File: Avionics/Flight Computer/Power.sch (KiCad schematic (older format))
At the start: 0 parts

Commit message: Lots of power tree and layout work
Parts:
- added C45: 1n, Capacitors_SMD:C_0402, symbol C
- added C46: 2.2u, Capacitors_SMD:C_0402, symbol C
- added C47: 0.1u, Capacitors_SMD:C_0402, symbol C
- added C48, C49: 10u, Capacitors_SMD:C_1206, symbol C
- added C50: 2.2u, Capacitors_SMD:C_0805, symbol C
- added C51, C52: 22u, Capacitors_SMD:C_1206, symbol C
- added L16, L17: 744316220, Inductors_SMD:L_Wuerth_HCI-5040, symbol L
- added R10: 20k, Resistors_SMD:R_0402, symbol R
- added R11: 12k, Resistors_SMD:R_0402, symbol R
- added R12: 100k, Resistors_SMD:R_0402, symbol R
- added R13: 10k, Resistors_SMD:R_0402, symbol R
- added U8: MAX17243, Housings_DFN_QFN:QFN-20-1EP_5x5mm_Pitch0.65mm, symbol MAX17243
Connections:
- new net: R11.1, U8.1 (FOSC)
- new net: C49.1, C50.1, L16.2, R12.1, U8.10 (SUP), U8.8 (SUPSW), U8.9 (SUPSW)
- new net: C47.2, U8.15 (BST)
- new net: C47.1, L17.2, U8.16 (LX), U8.17 (LX), U8.18 (LX)
- new net: R10.1, U8.4 (COMP)
- new net: C45.1, R10.2
- new net +3V3: C51.1, C52.1, L17.1, R13.1, U8.2 (OUT)
- new net BIAS: C46.1, U8.12 (SPS), U8.3 (FB), U8.5 (BIAS)
- new net GND: C45.2, C46.2, C48.2, C49.2, C50.2, C51.2, C52.2, R11.2, U8.13 (PGND), U8.14 (PGND), U8.20 (FSYNC), U8.21 (PGND_EP), U8.6 (AGND)
- new net PGOOD: R13.2, U8.11 (PGOOD)
- new net VIN: C48.1, L16.1
- new net ~SHDN: R12.2, U8.7 (EN)
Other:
- note added: "2.2uH, 5040 package Wurth"
- note added: "FSYNC tied low to enable pulse-frequency modulation"
- note added: "Input caps must be >=50V rated"
- note added: "Input pi filter (helps block ESC noise)"
- note added: "Note that SHDN is pulled high to VIN"
- note added: "R11 sets oscillation frequency to 2.2MHz"
- note added: "SPS and FB tied to bias to enable 3.3V spread spectrum mode."
- note added: "TODO: Tune input filter"

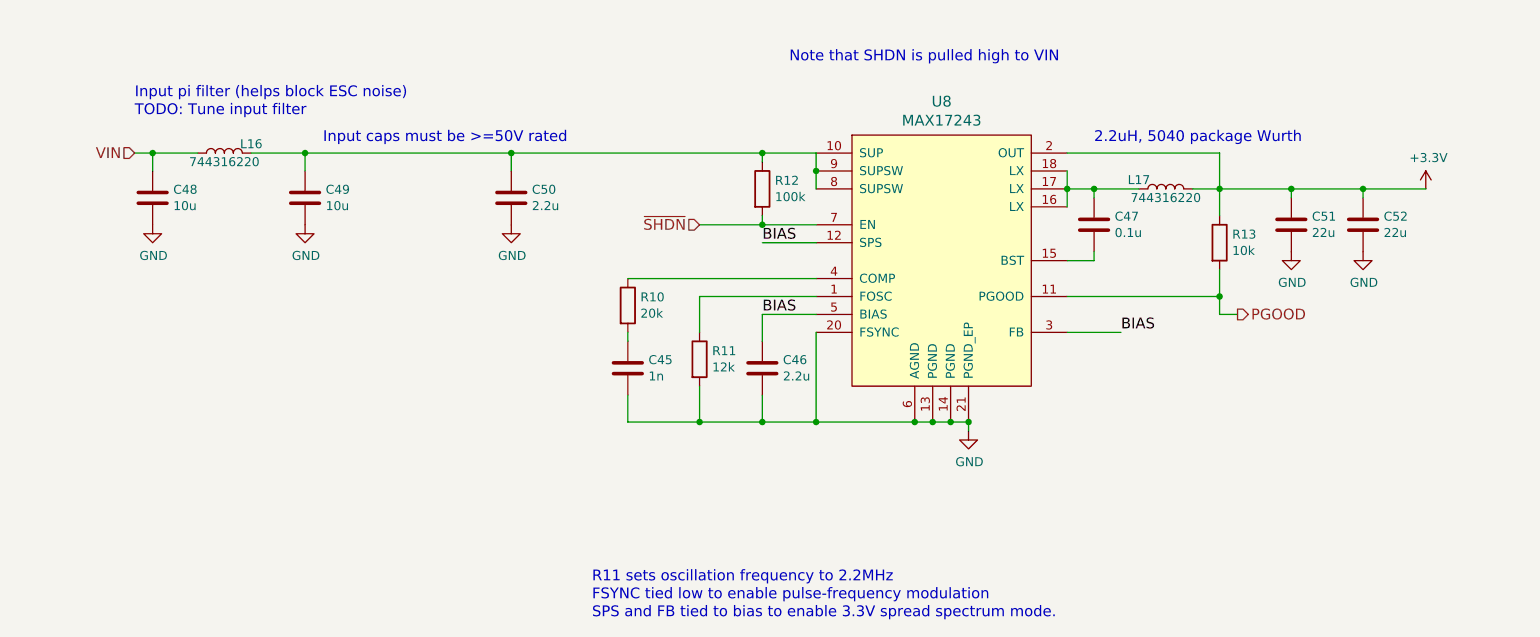
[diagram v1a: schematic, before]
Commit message: Restarted initial layout and cleaned up decoupling/RF layout.
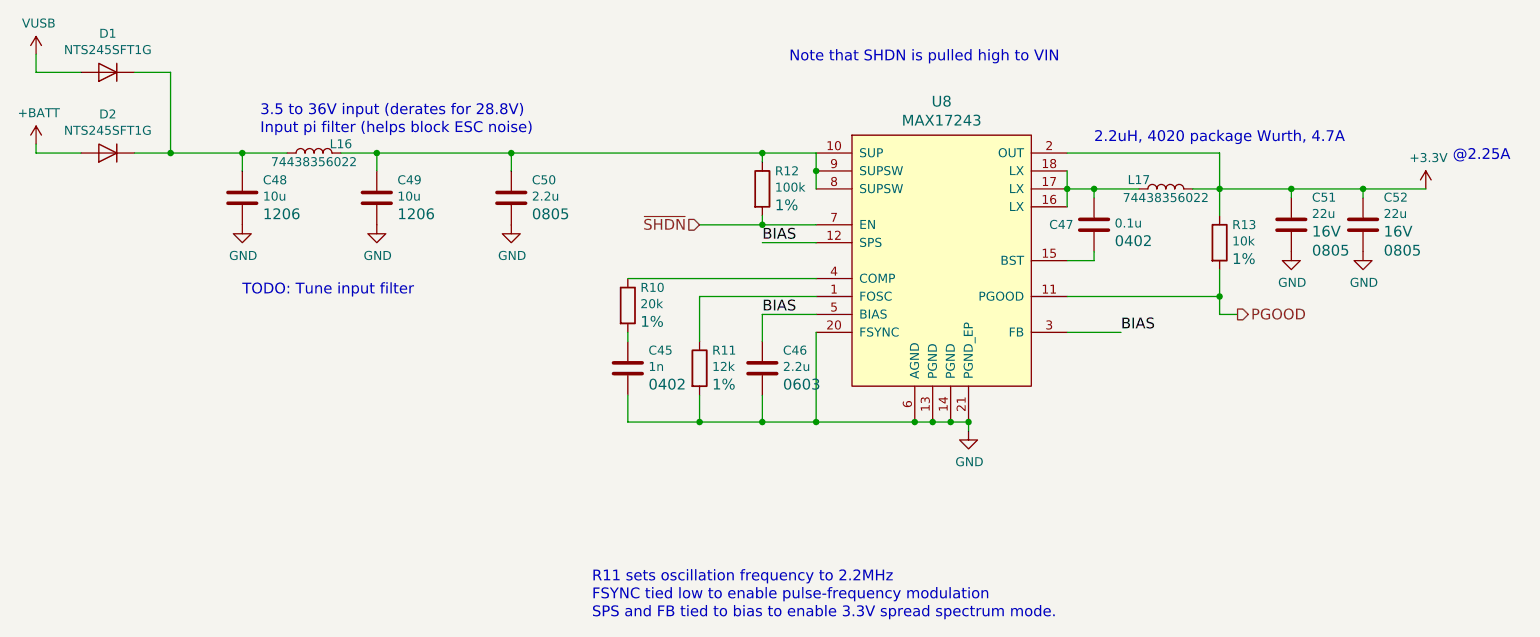
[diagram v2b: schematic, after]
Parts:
- added D1, D2: NTS245SFT1G, Diodes_SMD:D_SOD-123F, symbol D
- C45, C47: Package (none) -> 0402; Tolerance (none) -> 20%; Type (none) -> X7R; Voltage (none) -> 50V
- C46: footprint Capacitors_SMD:C_0402 -> Capacitors_SMD:C_0603; Package (none) -> 0603; Tolerance (none) -> 20%; Type (none) -> X7R; Voltage (none) -> 16V
- C48, C49: Package (none) -> 1206; Tolerance (none) -> 20%; Type (none) -> X7R; Voltage (none) -> 50V
- C50: Package (none) -> 0805; Tolerance (none) -> 20%; Type (none) -> X7R; Voltage (none) -> 50V
- C51, C52: footprint Capacitors_SMD:C_1206 -> Capacitors_SMD:C_0805; Package (none) -> 0805; Tolerance (none) -> 20%; Type (none) -> X7R; Voltage (none) -> 16V
- L16, L17: value 744316220 -> 74438356022; footprint Inductors_SMD:L_Wuerth_HCI-5040 -> Inductors_SMD:L_Wuerth_MAPI-4020
- R10, R11, R12, R13: Material (none) -> Thin Film; Package (none) -> 0402; Power (none) -> 0.062W; Tolerance (none) -> 1%; Voltage (none) -> 50V
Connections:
- net VIN: no longer names the net of C48.1, L16.1
- net VIN: now also D1.1 (K), D2.1 (K)
- new net +BATT: D2.2 (A)
- new net VUSB: D1.2 (A)
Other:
- note added: "2.2uH, 4020 package Wurth, 4.7A"
- note added: "3.5 to 36V input (derates for 28.8V)"
- note added: "@2.25A"
- note removed: "2.2uH, 5040 package Wurth"
- note removed: "Input caps must be >=50V rated"
- moved on the sheet: L16

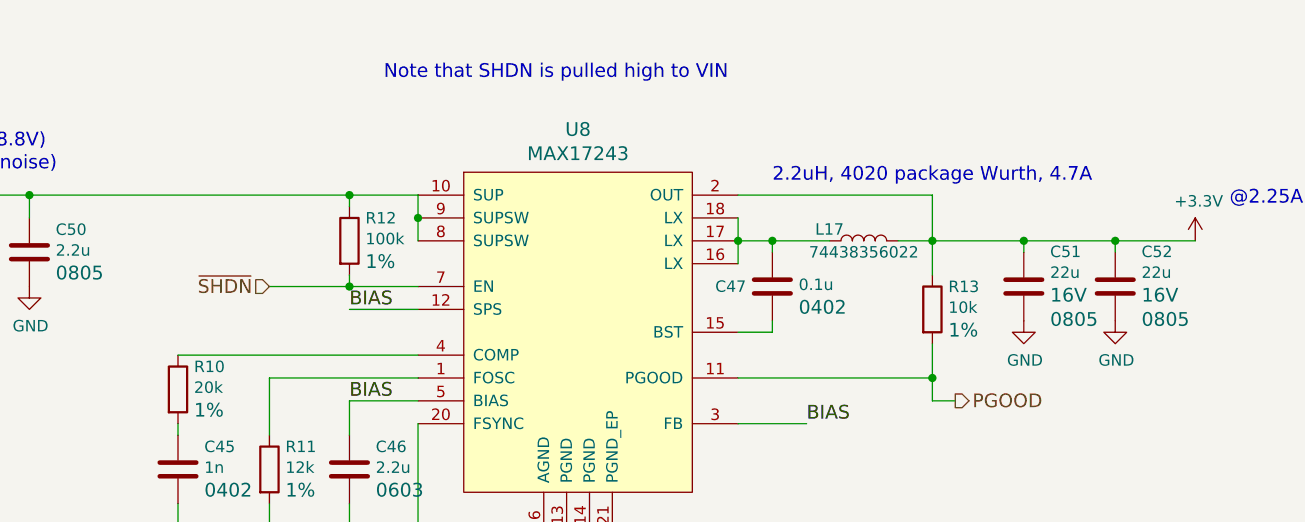
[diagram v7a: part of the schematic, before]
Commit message: Finished routing and DRC check.
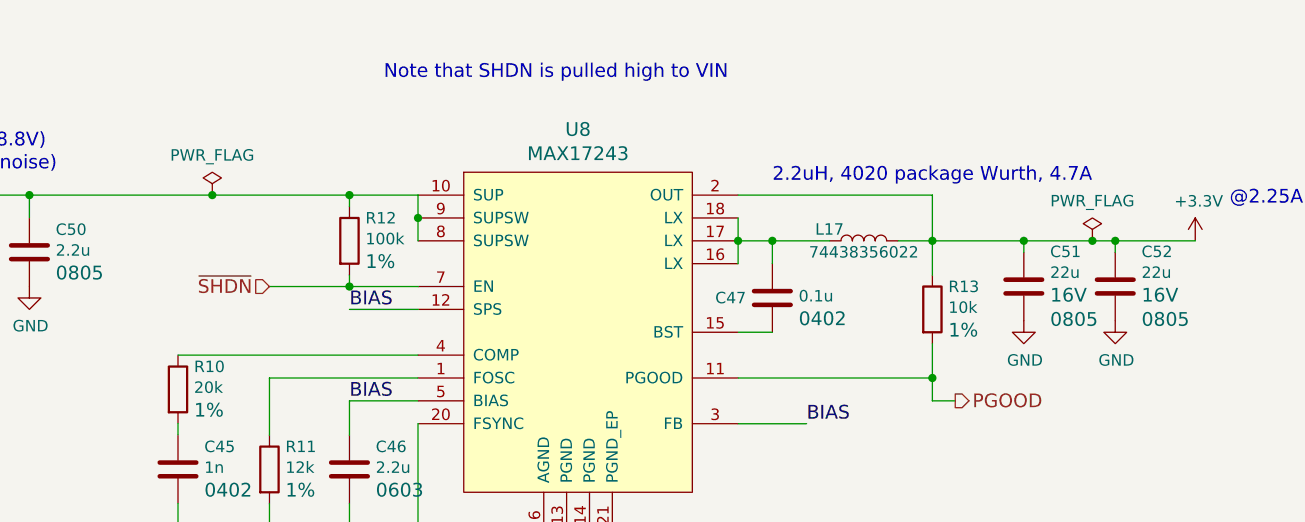
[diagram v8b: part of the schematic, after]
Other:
- moved on the sheet: C47
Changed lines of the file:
@@
 Text Notes 6750 2850 0    60   ~ 0
 2.2uH, 4020 package Wurth, 4.7A
-$Comp
-L MAX17243 U8
-U 1 1 58AB8A07
-P 5900 3500
-F 0 "U8" H 5900 4387 60  0000 C CNN
-F 1 "MAX17243" H 5900 4281 60  0000 C CNN
-F 2 "Housings_DFN_QFN:QFN-20-1EP_5x5mm_Pitch0.65mm" H 1150 1300 60  0001 C CNN
-F 3 "http://datasheets.maximintegrated.com/en/ds/MAX17242-MAX17243.pdf" H 1150 -800 60  0001 C CNN
-	1    5900 3500
-	1    0    0    -1
-$EndComp
 Text Label 6900 3900 0    60   ~ 0
 BIAS
@@
 BIAS
 $Comp
-L GND #PWR097
+L GND #PWR0111
 U 1 1 58AB8EE1
 P 6050 4450
-F 0 "#PWR097" H 2800 -350 50  0001 C CNN
+F 0 "#PWR0111" H 2800 -350 50  0001 C CNN
 F 1 "GND" H 6055 4277 50  0000 C CNN
 F 2 "" H 2800 -100 50  0001 C CNN
@@
 R11 sets oscillation frequency to 2.2MHz
 $Comp
-L +3.3V #PWR098
+L +3.3V #PWR0112
 U 1 1 58AB9BA4
 P 8600 3100
-F 0 "#PWR098" H 3600 0   50  0001 C CNN
+F 0 "#PWR0112" H 3600 0   50  0001 C CNN
 F 1 "+3.3V" H 8615 3273 50  0000 C CNN
 F 2 "" H 3600 150 50  0001 C CNN
@@
 PGOOD
 $Comp
-L GND #PWR099
+L GND #PWR0113
 U 1 1 58ABCF35
 P 3500 3300
-F 0 "#PWR099" H 250 -1500 50  0001 C CNN
+F 0 "#PWR0113" H 250 -1500 50  0001 C CNN
 F 1 "GND" H 3505 3127 50  0000 C CNN
 F 2 "" H 250 -1250 50  0001 C CNN
@@
 $EndComp
 $Comp
-L GND #PWR0100
+L GND #PWR0114
 U 1 1 58ABD05E
 P 2750 3300
-F 0 "#PWR0100" H -500 -1500 50  0001 C CNN
+F 0 "#PWR0114" H -500 -1500 50  0001 C CNN
 F 1 "GND" H 2755 3127 50  0000 C CNN
 F 2 "" H -500 -1250 50  0001 C CNN
@@
 	6600 3500 6750 3500
 Wire Wire Line
-	6750 3500 6750 3450
-Wire Wire Line
-	6750 3150 6750 3100
+	6750 3200 6750 3100
 Connection ~ 6750 3100
 Wire Wire Line
@@
 Connection ~ 2750 2900
 $Comp
-L GND #PWR0101
+L GND #PWR0115
 U 1 1 58ABDCB9
 P 2000 3300
-F 0 "#PWR0101" H -1250 -1500 50  0001 C CNN
+F 0 "#PWR0115" H -1250 -1500 50  0001 C CNN
 F 1 "GND" H 2005 3127 50  0000 C CNN
 F 2 "" H -1250 -1250 50  0001 C CNN
@@
 Connection ~ 8250 3100
 $Comp
-L GND #PWR0102
+L GND #PWR0116
 U 1 1 58ABEDD8
 P 7850 3450
-F 0 "#PWR0102" H 4600 -1350 50  0001 C CNN
+F 0 "#PWR0116" H 4600 -1350 50  0001 C CNN
 F 1 "GND" H 7855 3277 50  0000 C CNN
 F 2 "" H 4600 -1100 50  0001 C CNN
@@
 $EndComp
 $Comp
-L GND #PWR0103
+L GND #PWR0117
 U 1 1 58ABEEB5
 P 8250 3450
-F 0 "#PWR0103" H 5000 -1350 50  0001 C CNN
+F 0 "#PWR0117" H 5000 -1350 50  0001 C CNN
 F 1 "GND" H 8255 3277 50  0000 C CNN
 F 2 "" H 5000 -1100 50  0001 C CNN
@@
 	850  2450 850  2350
 $Comp
-L +BATT #PWR0104
+L +BATT #PWR0118
 U 1 1 58B2E558
 P 850 2850
-F 0 "#PWR0104" H -200 -50 50  0001 C CNN
+F 0 "#PWR0118" H -200 -50 50  0001 C CNN
 F 1 "+BATT" H 865 3023 50  0000 C CNN
 F 2 "" H -200 100 50  0001 C CNN
@@
 $EndComp
 $Comp
-L VUSB #PWR0105
+L VUSB #PWR0119
 U 1 1 58B2E98C
 P 850 2350
-F 0 "#PWR0105" H -300 250 50  0001 C CNN
+F 0 "#PWR0119" H -300 250 50  0001 C CNN
 F 1 "VUSB" H 865 2523 50  0000 C CNN
 F 2 "" H -300 400 50  0001 C CNN
@@
 L C C47
 U 1 1 58B74095
-P 6750 3300
-F 0 "C47" H 6500 3300 50  0000 L CNN
-F 1 "0.1u" H 6865 3308 50  0000 L CNN
-F 2 "Capacitors_SMD:C_0402" H 4888 -1100 50  0001 C CNN
-F 3 "" H 4850 -950 50  0001 C CNN
-F 4 "50V" H 4950 -1000 60  0001 L CNN "Voltage"
-F 5 "20%" H 4950 -900 60  0001 L CNN "Tolerance"
-F 6 "X7R" H 4900 -800 60  0001 L CNN "Type"
-F 7 "0402" H 6865 3209 60  0000 L CNN "Package"
-	1    6750 3300
+P 6750 3350
+F 0 "C47" H 6500 3350 50  0000 L CNN
+F 1 "0.1u" H 6865 3358 50  0000 L CNN
+F 2 "Capacitors_SMD:C_0402" H 4888 -1050 50  0001 C CNN
+F 3 "" H 4850 -900 50  0001 C CNN
+F 4 "50V" H 4950 -950 60  0001 L CNN "Voltage"
+F 5 "20%" H 4950 -850 60  0001 L CNN "Tolerance"
+F 6 "X7R" H 4900 -750 60  0001 L CNN "Type"
+F 7 "0402" H 6865 3259 60  0000 L CNN "Package"
+	1    6750 3350
 	1    0    0    -1
 $EndComp
@@
 	1    0    0    -1
 $EndComp
+$Comp
+L PWR_FLAG #FLG0120
+U 1 1 58BE5ADD
+P 8150 3100
+F 0 "#FLG0120" H 8200 3150 50  0001 C CNN
+F 1 "PWR_FLAG" H 8150 3274 50  0000 C CNN
+F 2 "" H -1500 550 50  0001 C CNN
+F 3 "" H -1500 550 50  0001 C CNN
+	1    8150 3100
+	1    0    0    -1
+$EndComp
+Connection ~ 8150 3100
+$Comp
+L PWR_FLAG #FLG0121
+U 1 1 58BE6F80
+P 4300 2900
+F 0 "#FLG0121" H 0   925 50  0001 C CNN
+F 1 "PWR_FLAG" H 4300 3074 50  0000 C CNN
+F 2 "" H 0   850 50  0001 C CNN
+F 3 "" H 0   850 50  0001 C CNN
+	1    4300 2900
+	1    0    0    -1
+$EndComp
+Connection ~ 4300 2900
+$Comp
+L MAX17243 U8
+U 1 1 58BF5C45
+P 5900 3500
+F 0 "U8" H 5900 4387 60  0000 C CNN
+F 1 "MAX17243" H 5900 4281 60  0000 C CNN
+F 2 "Housings_DFN_QFN:QFN-20-1EP_5x5mm_Pitch0.65mm" H -2550 2100 60  0001 C CNN
+F 3 "http://datasheets.maximintegrated.com/en/ds/MAX17242-MAX17243.pdf" H -2550 0   60  0001 C CNN
+	1    5900 3500
+	1    0    0    -1
+$EndComp
